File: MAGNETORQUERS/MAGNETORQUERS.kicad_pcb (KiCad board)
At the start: 2 copper layers, 32.4 x 20.2 mm, 13 parts, among them U1 DRV8876PWPR

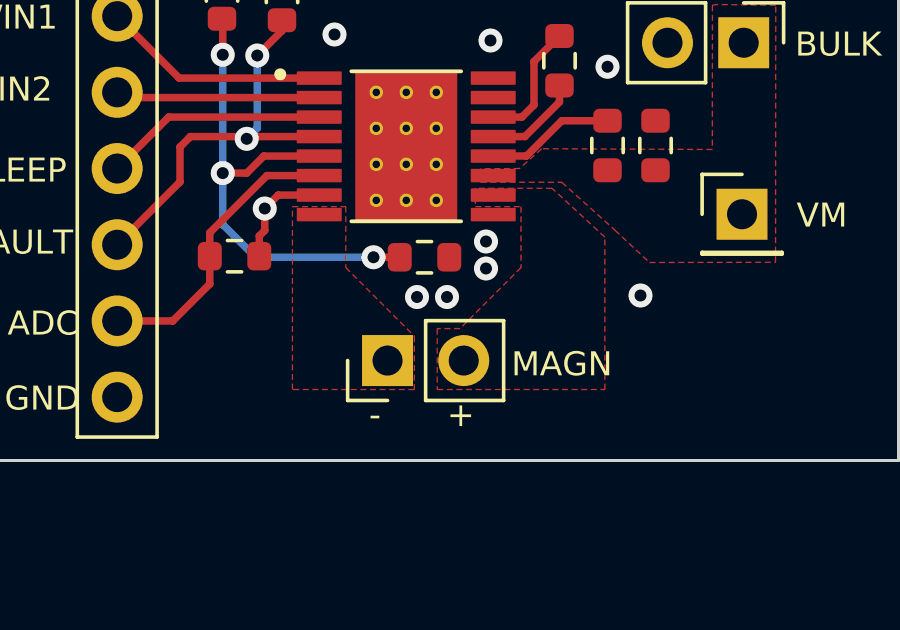
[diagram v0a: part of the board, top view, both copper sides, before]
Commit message: connected drv middle thermal pad to ground (it wasn't connected to anything)
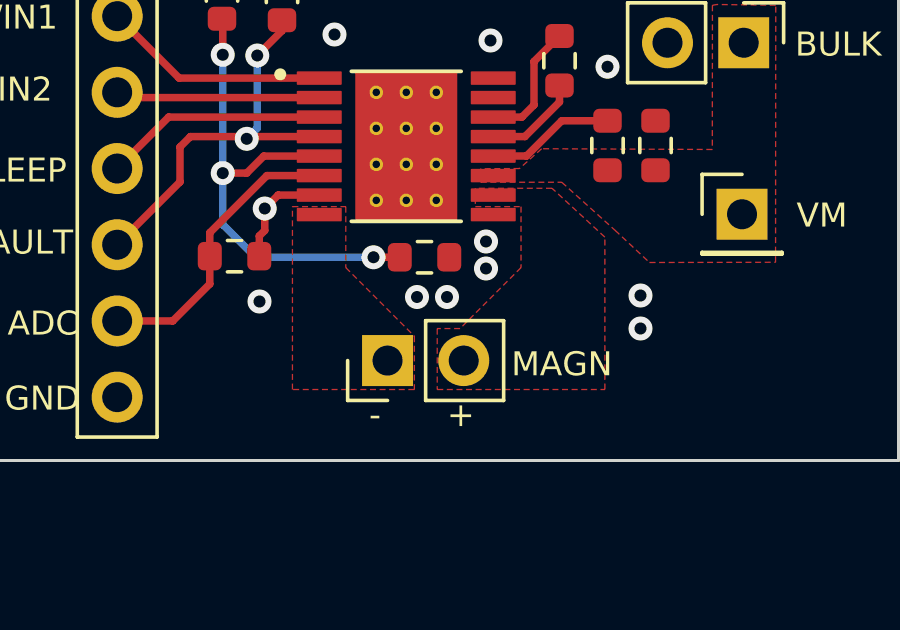
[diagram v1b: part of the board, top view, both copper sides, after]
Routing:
- net Earth: vias 9 -> 11
